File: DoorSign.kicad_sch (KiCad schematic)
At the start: 41 parts, among them J1 Wall, J2 Taster A, J3 Taster-LED, J4 Taster B, U1 Pico, U2 PC817, U3 LM2575-5.0BT

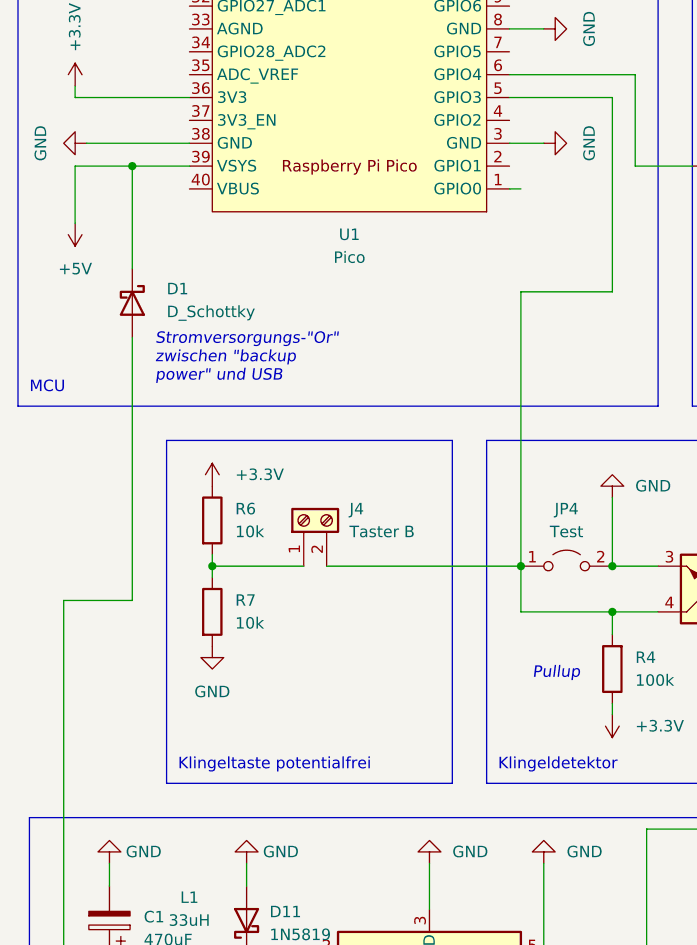
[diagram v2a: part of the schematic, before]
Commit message: Jumpers for potential free contact
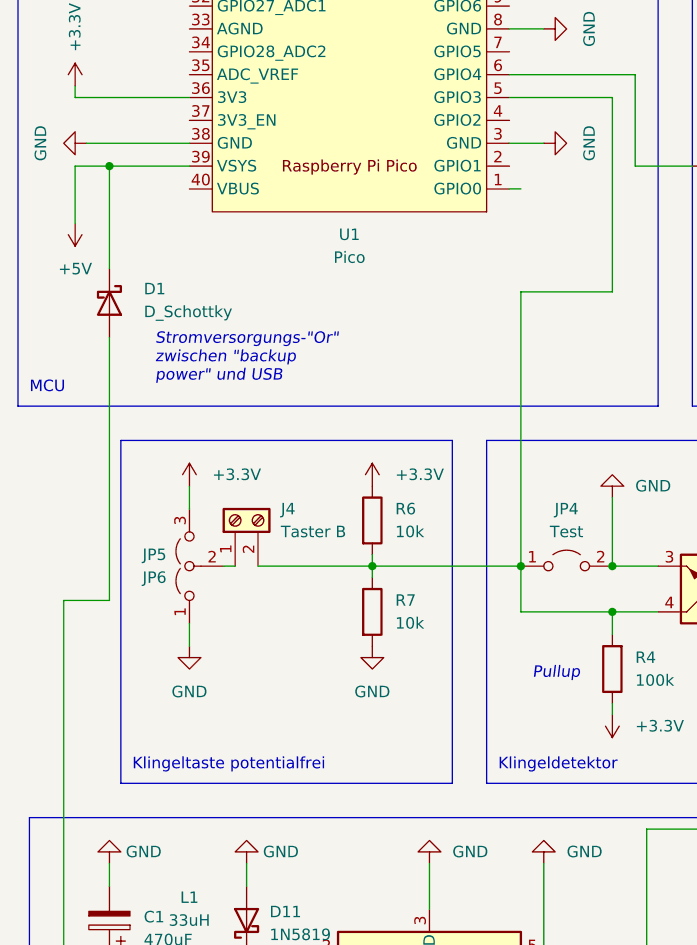
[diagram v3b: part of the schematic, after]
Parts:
- added JP5: JP6, Connector_PinHeader_2.54mm:PinHeader_1x03_P2.54mm_Vertical, symbol Jumper:Jumper_3_Open
- JP4: footprint TestPoint:TestPoint_2Pads_Pitch2.54mm_Drill0.8mm -> Connector_PinHeader_2.54mm:PinHeader_1x02_P2.54mm_Vertical
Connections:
- net +3.3V: now also JP5.3 (B)
- net GND: now also JP5.1 (A)
- net at J4.2 (Pin_2), JP4.1 (A), R4.2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: now also R6.2, R7.1
- new net: J4.1 (Pin_1), JP5.2 (C)
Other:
- moved on the sheet: D1, J4, R6, R7
